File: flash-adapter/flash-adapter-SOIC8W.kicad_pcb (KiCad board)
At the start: 2 copper layers, 10 x 8.5 mm, 3 parts, among them J101 Conn_02x04_Odd_Even, U101 W25Q64FVSS

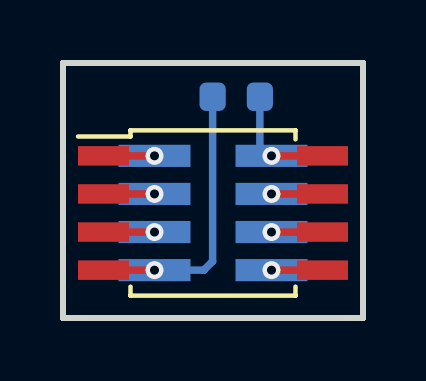
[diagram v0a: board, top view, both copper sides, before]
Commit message: increase trace width
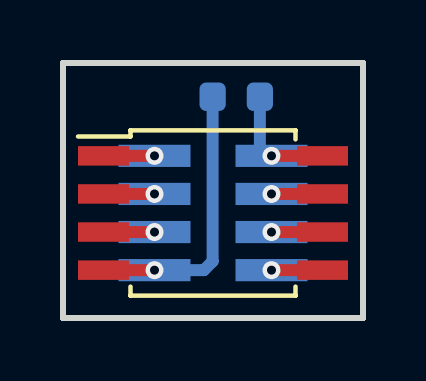
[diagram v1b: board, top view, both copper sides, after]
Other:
- net class Default: trace_width 0.25 -> 0.4
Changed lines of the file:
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@@
   )
   (setup
-    (last_trace_width 0.25)
+    (last_trace_width 0.4)
     (trace_clearance 0.25)
     (zone_clearance 0.508)
@@
   (net_class Default "This is the default net class."
     (clearance 0.25)
-    (trace_width 0.25)
+    (trace_width 0.4)
     (via_dia 0.6)
     (via_drill 0.3)
@@
   (gr_line (start 105 95) (end 105 103.5) (layer Edge.Cuts) (width 0.2))
   (gr_line (start 95 95) (end 105 95) (layer Edge.Cuts) (width 0.2))
-  (segment (start 96.35 98.095) (end 98.05 98.095) (width 0.25) (layer F.Cu) (net 1) (status 10))
+  (segment (start 96.35 98.095) (end 98.05 98.095) (width 0.4) (layer F.Cu) (net 1) (status 10))
   (via (at 98.05 98.095) (size 0.6) (drill 0.3) (layers F.Cu B.Cu) (net 1) (status 30))
   (via (at 98.05 99.365) (size 0.6) (drill 0.3) (layers F.Cu B.Cu) (net 2) (status 30))
-  (segment (start 96.35 99.365) (end 98.05 99.365) (width 0.25) (layer F.Cu) (net 2) (status 10))
+  (segment (start 96.35 99.365) (end 98.05 99.365) (width 0.4) (layer F.Cu) (net 2) (status 10))
   (via (at 98.05 100.635) (size 0.6) (drill 0.3) (layers F.Cu B.Cu) (net 3) (status 30))
-  (segment (start 96.35 100.635) (end 98.05 100.635) (width 0.25) (layer F.Cu) (net 3) (status 10))
+  (segment (start 96.35 100.635) (end 98.05 100.635) (width 0.4) (layer F.Cu) (net 3) (status 10))
   (via (at 98.05 101.905) (size 0.6) (drill 0.3) (layers F.Cu B.Cu) (net 4))
-  (segment (start 96.35 101.905) (end 98.05 101.905) (width 0.25) (layer F.Cu) (net 4))
-  (segment (start 99.9875 96.125) (end 99.9875 101.6125) (width 0.25) (layer B.Cu) (net 4))
-  (segment (start 99.695 101.905) (end 98.05 101.905) (width 0.25) (layer B.Cu) (net 4))
-  (segment (start 99.9875 101.6125) (end 99.695 101.905) (width 0.25) (layer B.Cu) (net 4))
+  (segment (start 96.35 101.905) (end 98.05 101.905) (width 0.4) (layer F.Cu) (net 4))
+  (segment (start 99.9875 96.125) (end 99.9875 101.6125) (width 0.4) (layer B.Cu) (net 4))
+  (segment (start 99.695 101.905) (end 98.05 101.905) (width 0.4) (layer B.Cu) (net 4))
+  (segment (start 99.9875 101.6125) (end 99.695 101.905) (width 0.4) (layer B.Cu) (net 4))
   (via (at 101.95 101.905) (size 0.6) (drill 0.3) (layers F.Cu B.Cu) (net 5) (status 30))
-  (segment (start 103.65 101.905) (end 101.95 101.905) (width 0.25) (layer F.Cu) (net 5) (status 10))
+  (segment (start 103.65 101.905) (end 101.95 101.905) (width 0.4) (layer F.Cu) (net 5) (status 10))
   (via (at 101.95 100.635) (size 0.6) (drill 0.3) (layers F.Cu B.Cu) (net 6) (status 30))
-  (segment (start 103.65 100.635) (end 101.95 100.635) (width 0.25) (layer F.Cu) (net 6) (status 10))
+  (segment (start 103.65 100.635) (end 101.95 100.635) (width 0.4) (layer F.Cu) (net 6) (status 10))
   (via (at 101.95 99.365) (size 0.6) (drill 0.3) (layers F.Cu B.Cu) (net 7) (status 30))
-  (segment (start 103.65 99.365) (end 101.95 99.365) (width 0.25) (layer F.Cu) (net 7) (status 10))
+  (segment (start 103.65 99.365) (end 101.95 99.365) (width 0.4) (layer F.Cu) (net 7) (status 10))
   (via (at 101.95 98.095) (size 0.6) (drill 0.3) (layers F.Cu B.Cu) (net 8))
-  (segment (start 103.65 98.095) (end 101.95 98.095) (width 0.25) (layer F.Cu) (net 8))
-  (segment (start 101.945 98.1) (end 101.95 98.095) (width 0.25) (layer B.Cu) (net 8))
-  (segment (start 101.65 98.1) (end 101.945 98.1) (width 0.25) (layer B.Cu) (net 8))
-  (segment (start 101.5625 98.0125) (end 101.65 98.1) (width 0.25) (layer B.Cu) (net 8))
-  (segment (start 101.5625 96.125) (end 101.5625 98.0125) (width 0.25) (layer B.Cu) (net 8))
+  (segment (start 103.65 98.095) (end 101.95 98.095) (width 0.4) (layer F.Cu) (net 8))
+  (segment (start 101.945 98.1) (end 101.95 98.095) (width 0.4) (layer B.Cu) (net 8))
+  (segment (start 101.65 98.1) (end 101.945 98.1) (width 0.4) (layer B.Cu) (net 8))
+  (segment (start 101.5625 98.0125) (end 101.65 98.1) (width 0.4) (layer B.Cu) (net 8))
+  (segment (start 101.5625 96.125) (end 101.5625 98.0125) (width 0.4) (layer B.Cu) (net 8))
 )

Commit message: remove pin 1 markers from wrong position
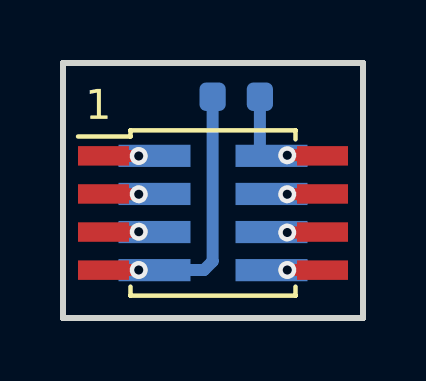
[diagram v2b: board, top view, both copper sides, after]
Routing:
- net /VCC: track 4.01 -> 3.20 mm
- net /~CS: track 1.70 -> 1.18 mm
- net /DQ0: track 1.70 -> 1.18 mm
- net /~WP: track 1.70 -> 1.18 mm
- net /~HOLD: track 1.70 -> 1.18 mm
- net /DQ1: track 1.70 -> 1.18 mm
- net /CLK: track 1.70 -> 1.18 mm
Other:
- board text added: "1"

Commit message: update pad to mask clearance
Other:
- rule pad_to_mask_clearance: 0.2 -> 0.1
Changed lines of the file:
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@@
     (pad_size 1.524 1.524)
     (pad_drill 0.762)
-    (pad_to_mask_clearance 0.2)
+    (pad_to_mask_clearance 0.1)
     (aux_axis_origin 0 0)
     (visible_elements FFFFFF7F)
